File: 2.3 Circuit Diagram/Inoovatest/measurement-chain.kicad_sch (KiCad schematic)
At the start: 37 parts, among them IC2 MAX6126, J3 M12 5-pin, Q6 AO3401A, Q7 AO3400A, Q8 AO3401A, Q9 AO3400A, U13 AD8421, U14 MCP41U83, U15 OPA188, U16 ADS127L02

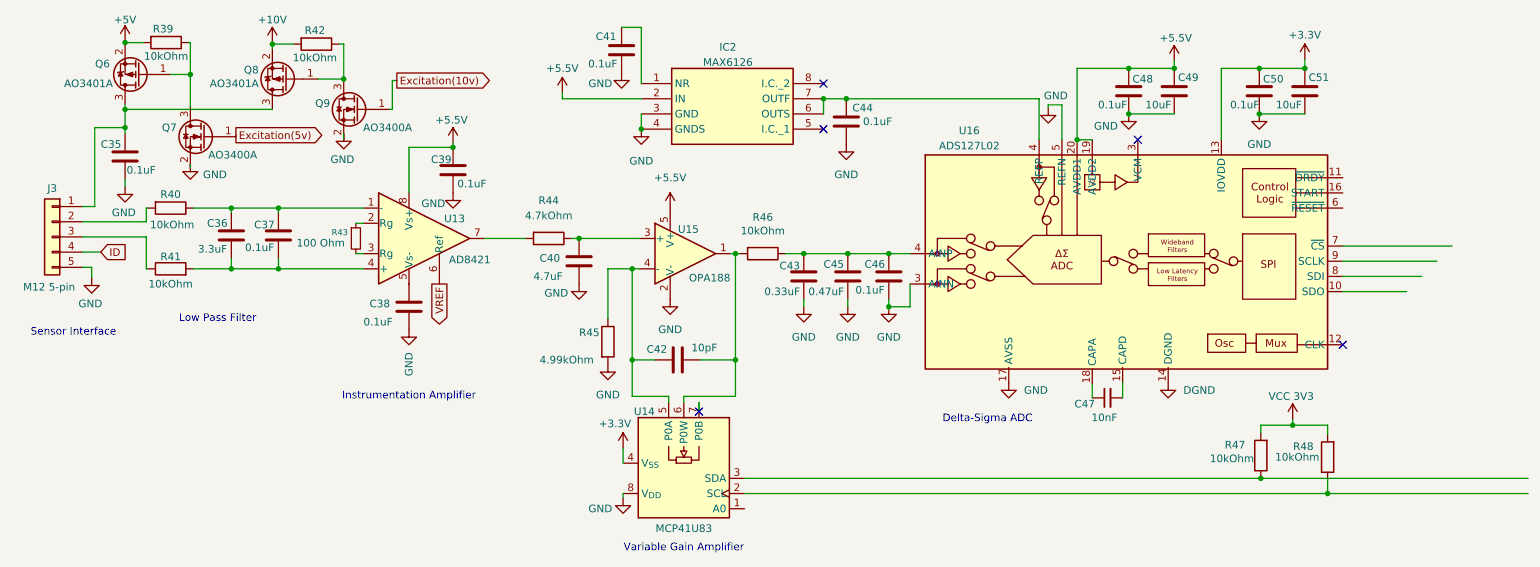
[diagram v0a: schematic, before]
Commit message: more datasheets
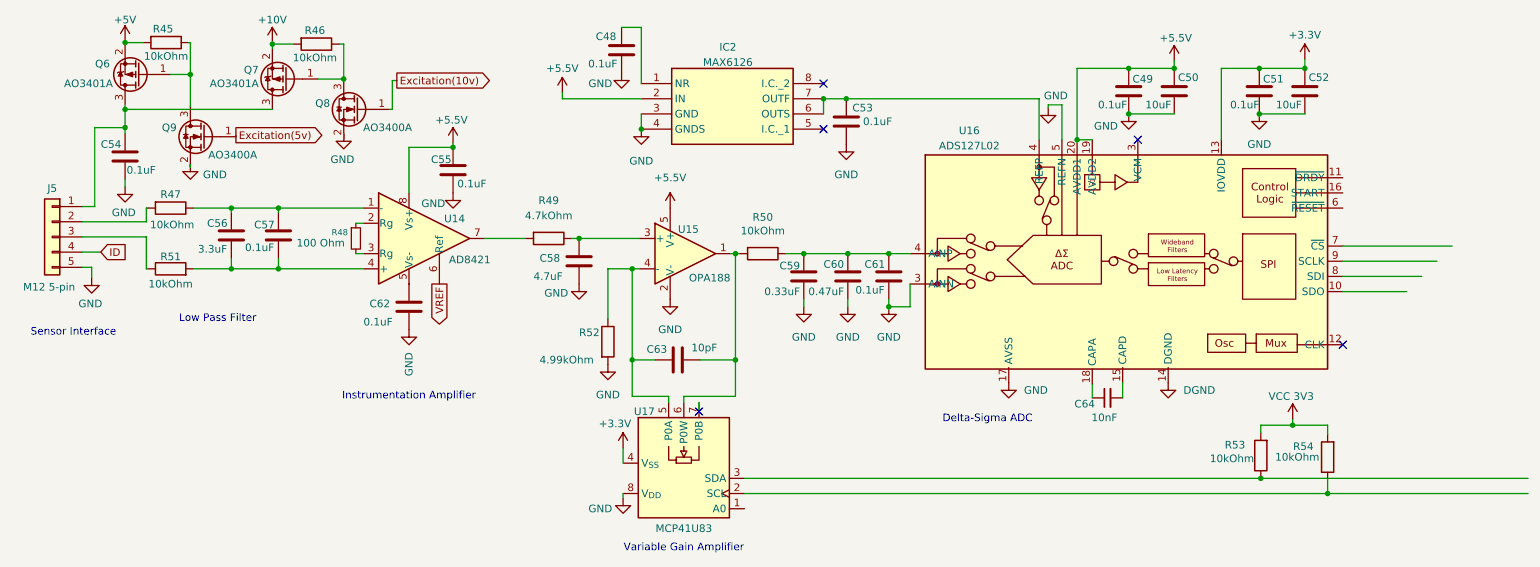
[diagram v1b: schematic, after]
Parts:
- renumbered C41 to C48, C48 to C49, C49 to C50, C50 to C51, C51 to C52, C44 to C53, C35 to C54, C39 to C55, C36 to C56, C37 to C57, C40 to C58, C43 to C59, C45 to C60, C46 to C61, C38 to C62, C42 to C63, C47 to C64, J3 to J5, Q8 to Q7, Q9 to Q8, Q7 to Q9, R39 to R45, R42 to R46, R40 to R47, R43 to R48, R44 to R49, R46 to R50, R41 to R51, R45 to R52, R47 to R53, R48 to R54, U13 to U14, U14 to U17
